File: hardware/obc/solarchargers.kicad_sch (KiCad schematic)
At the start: 36 parts, among them U105 LTC4121, U106 LTC4121

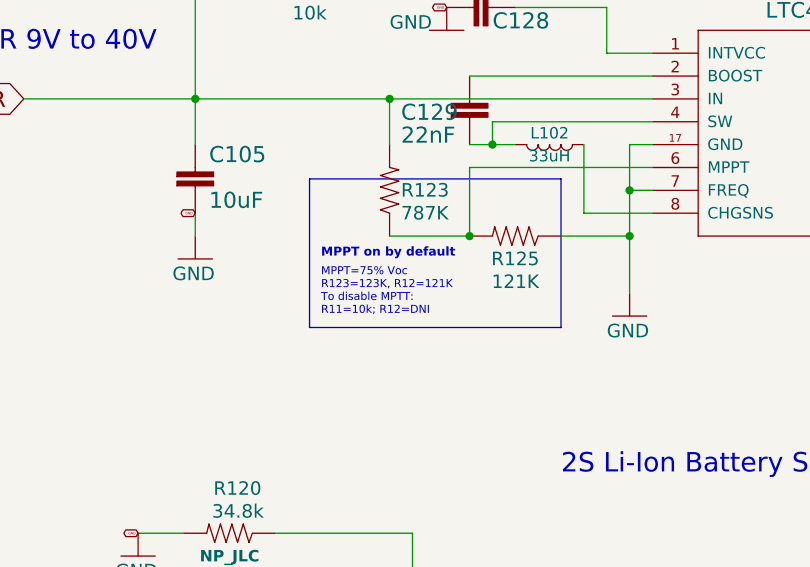
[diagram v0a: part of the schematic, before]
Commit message: obc: final (hopefully) design review for rev B
- Update some text
- Change some part values based on math (greater charge current)
- Increase design conservatism (place pullups on CS)

BOM review still needs to occur, including for a few parts that had
values changed in this pass (without part numbers being chosen)
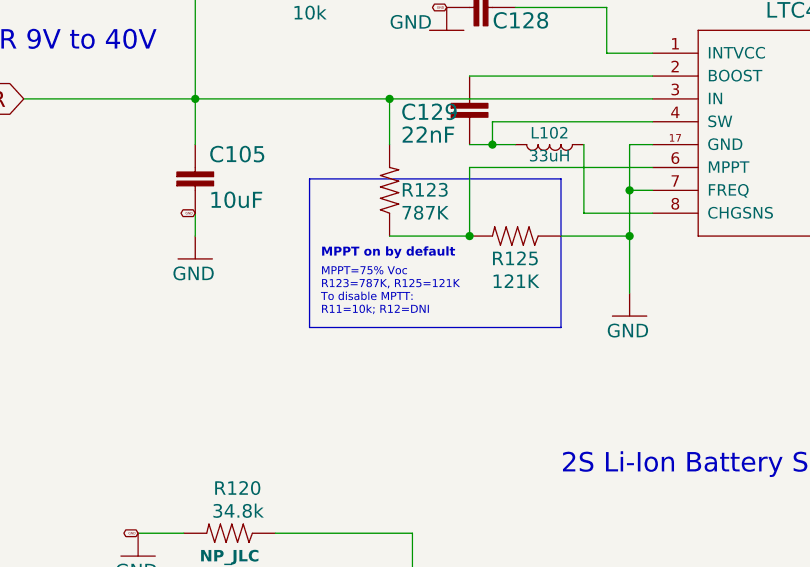
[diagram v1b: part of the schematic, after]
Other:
- note added: "MPPT=75% Voc R123=787K, R125=121K To disable MPTT: R11=10k; R12=DNI"
- note removed: "MPPT=75% Voc R123=123K, R12=121K To disable MPTT: R11=10k; R12=DNI"
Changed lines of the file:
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@@
 		)
 	)
-	(text "\nMPPT=75% Voc\nR123=123K, R12=121K\nTo disable MPTT:\nR11=10k; R12=DNI"
+	(text "\nMPPT=75% Voc\nR123=787K, R125=121K\nTo disable MPTT:\nR11=10k; R12=DNI"
 		(exclude_from_sim no)
 		(at 63.5 73.66 0)

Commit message: obc: final review of BOM
- fixed duplicate parts
- created new footprint for solar charger inductors
- changed LCSC part number for red LED because it no longer existed
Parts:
- L102, L103: footprint SSE_Footprints:TDK_1008_4.9x5.5mm -> NyanSat_Footprints:TDK VLCF5020T-330MR62-1; LCSC C2046704 -> C2043695; Manufacturer_Name TDK -> (none)
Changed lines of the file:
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@@
 			)
 		)
-		(property "Footprint" "SSE_Footprints:TDK_1008_4.9x5.5mm"
+		(property "Footprint" "NyanSat_Footprints:TDK VLCF5020T-330MR62-1"
 			(at 90.17 125.73 0)
 			(effects
@@
 			)
 		)
-		(property "Manufacturer_Name" "TDK"
+		(property "Manufacturer_Name" ""
 			(at 90.17 125.73 0)
 			(effects
@@
 			)
 		)
-		(property "LCSC" "C2046704"
+		(property "LCSC" "C2043695"
 			(at 90.17 125.73 0)
 			(effects
@@
 			)
 		)
-		(property "Description" "0 0603"
+		(property "Description" ""
 			(at 62.23 39.878 0)
 			(effects
@@
 			)
 		)
-		(property "Description" "0 0603"
+		(property "Description" ""
 			(at 63.5 110.998 0)
 			(effects
@@
 			)
 		)
-		(property "Footprint" "SSE_Footprints:TDK_1008_4.9x5.5mm"
+		(property "Footprint" "NyanSat_Footprints:TDK VLCF5020T-330MR62-1"
 			(at 88.9 54.61 0)
 			(effects
@@
 			)
 		)
-		(property "Manufacturer_Name" "TDK"
+		(property "Manufacturer_Name" ""
 			(at 88.9 54.61 0)
 			(effects
@@
 			)
 		)
-		(property "LCSC" "C2046704"
+		(property "LCSC" "C2043695"
 			(at 88.9 54.61 0)
 			(effects
